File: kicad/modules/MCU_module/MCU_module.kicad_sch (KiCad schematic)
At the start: 2 parts, among them J1 Screw_Terminal_01x20, J2 Screw_Terminal_01x20

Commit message: Connector for bigger current, control module 2
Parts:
- J1, J2: Mouser number (none) -> 649-68000-420HLF
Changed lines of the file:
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@@
 			)
 		)
-		(property "Description" "Generic screw terminal, single row, 01x20, script generated (kicad-library-utils/schlib/autogen/connector/)"
+		(property "Description" ""
+			(at 62.23 58.42 0)
+			(effects
+				(font
+					(size 1.27 1.27)
+				)
+				(hide yes)
+			)
+		)
+		(property "Manufacturer Part Number" ""
+			(at 62.23 58.42 0)
+			(effects
+				(font
+					(size 1.27 1.27)
+				)
+				(hide yes)
+			)
+		)
+		(property "Mouser number" "649-68000-420HLF"
 			(at 62.23 58.42 0)
 			(effects
@@
 			)
 		)
-		(property "Description" "Generic screw terminal, single row, 01x20, script generated (kicad-library-utils/schlib/autogen/connector/)"
-			(at 140.97 58.42 0)
-			(effects
+		(property "Description" ""
+			(at 140.97 58.42 0)
+			(effects
+				(font
+					(size 1.27 1.27)
+				)
+				(hide yes)
+			)
+		)
+		(property "Manufacturer Part Number" ""
+			(at 140.97 58.42 0)
+			(effects
+				(font
+					(size 1.27 1.27)
+				)
+				(hide yes)
+			)
+		)
+		(property "Mouser number" "649-68000-420HLF"
+			(at 140.97 58.42 0)
+			(effects

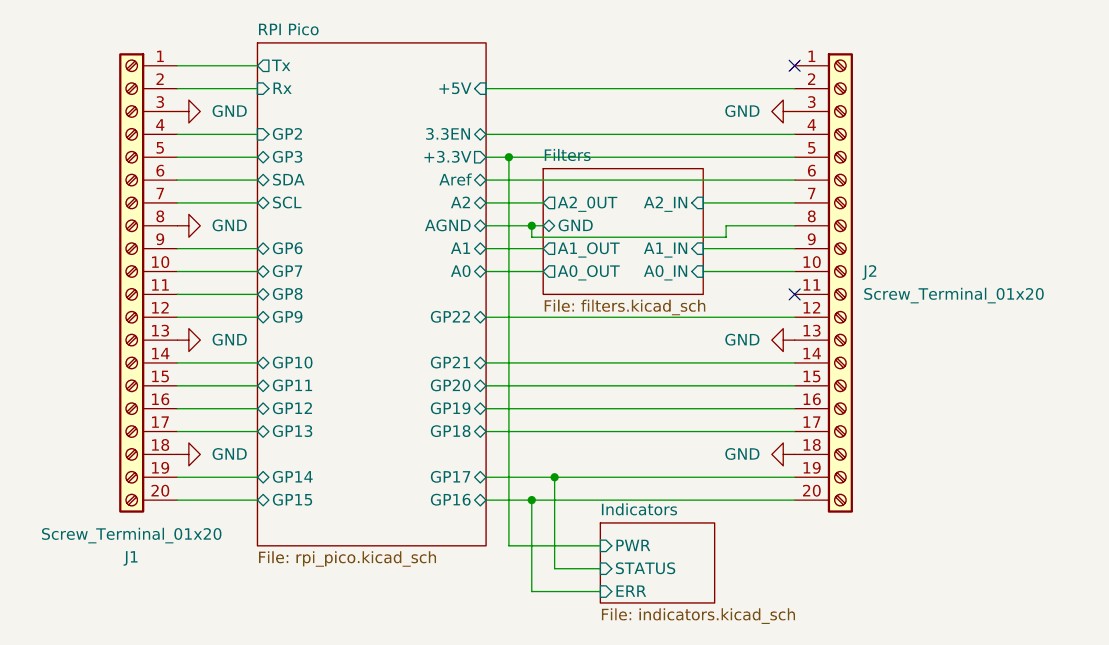
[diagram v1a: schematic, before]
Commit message: Add part numbers
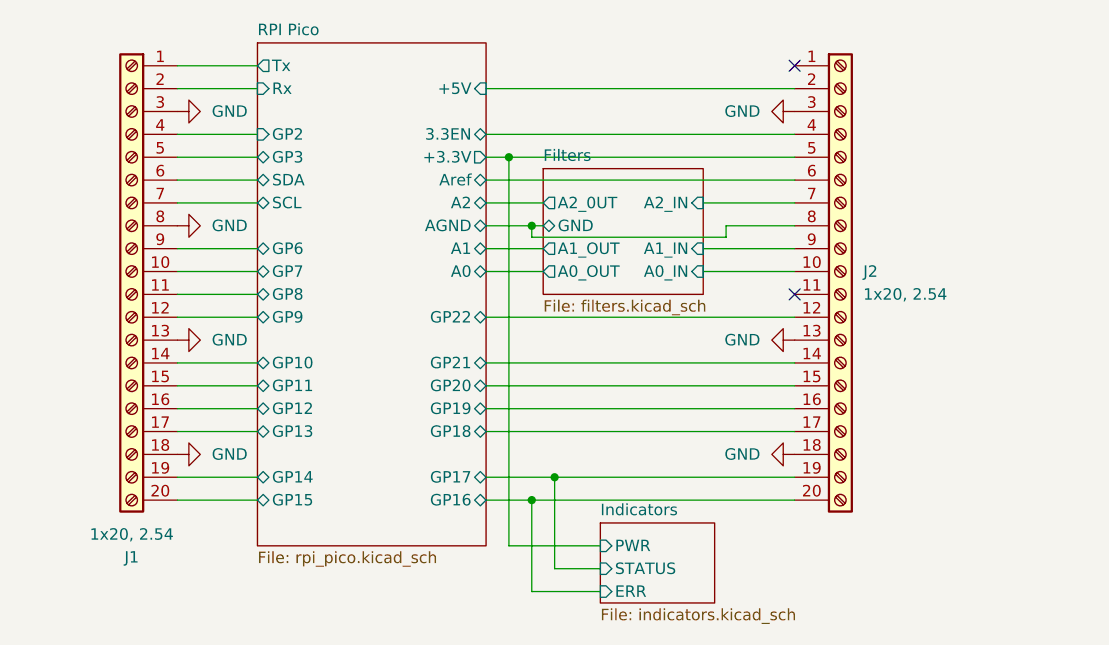
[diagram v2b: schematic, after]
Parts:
- J1, J2: value Screw_Terminal_01x20 -> 1x20, 2.54; Manufacturer Part Number (none) -> 68000-420HLF
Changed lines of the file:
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@@
 			)
 		)
-		(property "Value" "Screw_Terminal_01x20"
+		(property "Value" "1x20, 2.54"
 			(at 62.23 87.63 0)
 			(effects
@@
 			)
 		)
-		(property "Description" ""
-			(at 62.23 58.42 0)
-			(effects
-				(font
-					(size 1.27 1.27)
-				)
-				(hide yes)
-			)
-		)
-		(property "Manufacturer Part Number" ""
+		(property "Description" "CUSTOM"
+			(at 62.23 58.42 0)
+			(effects
+				(font
+					(size 1.27 1.27)
+				)
+				(hide yes)
+			)
+		)
+		(property "Manufacturer Part Number" "68000-420HLF"
 			(at 62.23 58.42 0)
 			(effects
@@
 			)
 		)
-		(property "Value" "Screw_Terminal_01x20"
+		(property "Value" "1x20, 2.54"
 			(at 143.51 60.9599 0)
 			(effects
@@
 			)
 		)
-		(property "Description" ""
-			(at 140.97 58.42 0)
-			(effects
-				(font
-					(size 1.27 1.27)
-				)
-				(hide yes)
-			)
-		)
-		(property "Manufacturer Part Number" ""
-			(at 140.97 58.42 0)
-			(effects
+		(property "Description" "CUSTOM"
+			(at 140.97 58.42 0)
+			(effects
+				(font
+					(size 1.27 1.27)
+				)
+				(hide yes)
+			)
+		)
+		(property "Manufacturer Part Number" "68000-420HLF"
+			(at 140.97 58.42 0)
+			(effects
